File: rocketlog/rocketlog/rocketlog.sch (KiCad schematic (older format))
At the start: 14 parts, among them J1 Conn_01x05_Female, U1 DSPIC33EP512GP502, U2 MCP2562, Y1 Crystal

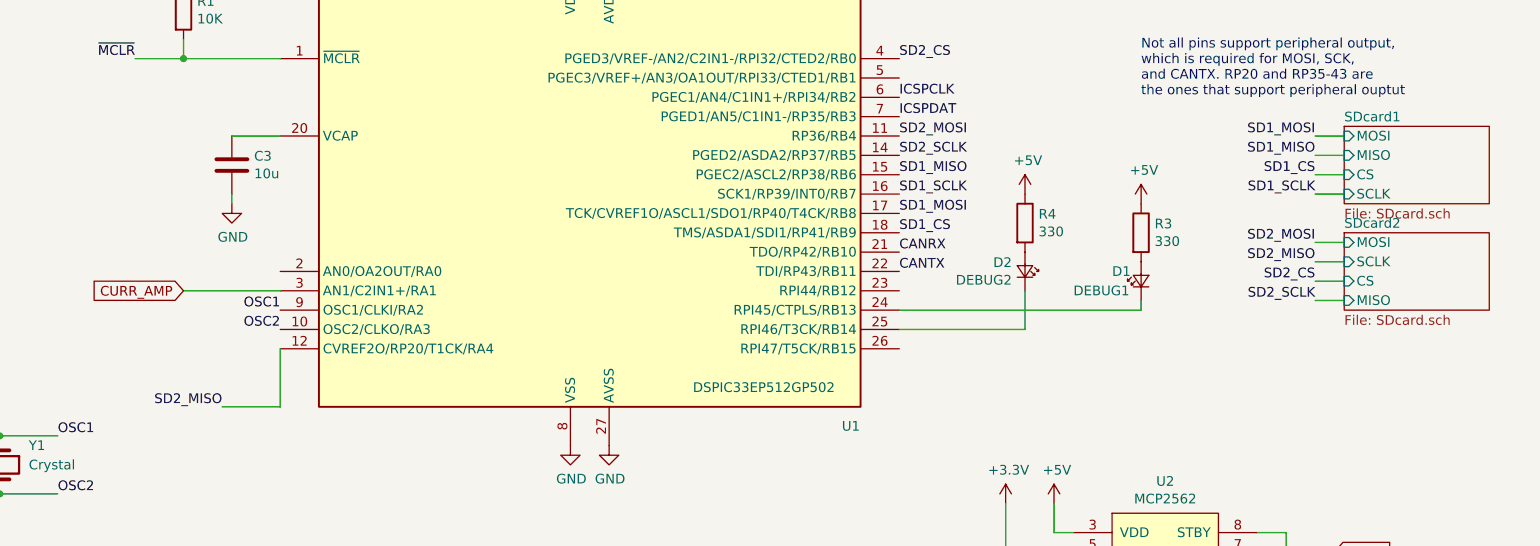
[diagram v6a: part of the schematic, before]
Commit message: Logger Board: Add pullup resistors on SD card MISO lines
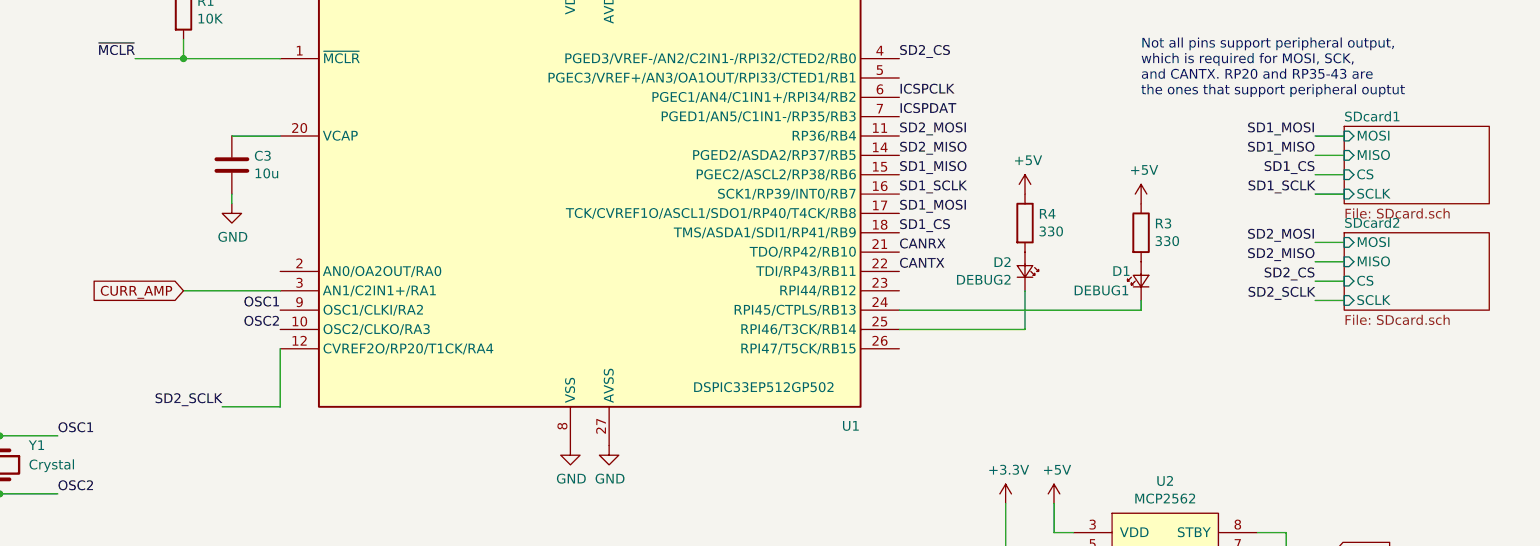
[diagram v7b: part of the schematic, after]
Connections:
- net SD2_MISO: now also U1.14 (PGED2/ASDA2/RP37/RB5); no longer U1.12 (CVREF2O/RP20/T1CK/RA4)
- net SD2_SCLK: now also U1.12 (CVREF2O/RP20/T1CK/RA4); no longer U1.14 (PGED2/ASDA2/RP37/RB5)
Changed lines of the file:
@@
 F0 "SDcard2" 50
 F1 "SDcard.sch" 50
-F2 "MISO" I L 9700 4500 50
+F2 "MISO" I L 9700 4300 50
 F3 "MOSI" I L 9700 4200 50
-F4 "SCLK" I L 9700 4300 50
+F4 "SCLK" I L 9700 4500 50
 F5 "CS" I L 9700 4400 50
 $EndSheet
@@
 Text Label 7400 3650 0    50   ~ 0
 SD2_MOSI
-Text Label 3900 5050 2    50   ~ 0
+Text Label 7400 3750 0    50   ~ 0
 SD2_MISO
 Text Label 7400 3250 0    50   ~ 0
 SD2_CS
-Text Label 7400 3750 0    50   ~ 0
+Text Label 3900 5050 2    50   ~ 0
 SD2_SCLK
 Text Label 7400 4350 0    50   ~ 0

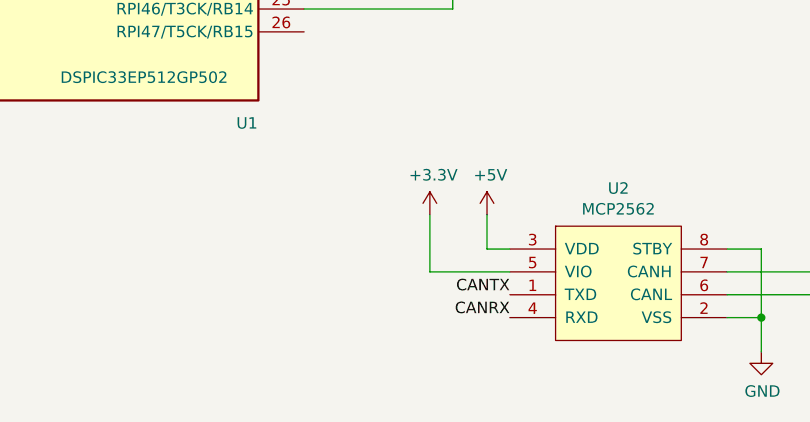
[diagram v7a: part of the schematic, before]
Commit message: Logger Board: Fab review 1 fixes
Changes fixed in this commit:
  - Make mounting holes 1.5in square because I ain't no metric apologist
  - Make programming header not overhang bottom right mounting hole
  - Change MCLR to ~MCLR on silkscreen
  - Move C1 closer to MCU
  - Move C3 further from MCU
  - Add 10uF capacitor on CAN transceiver (C11)

Generate gerbers to reflect these changes
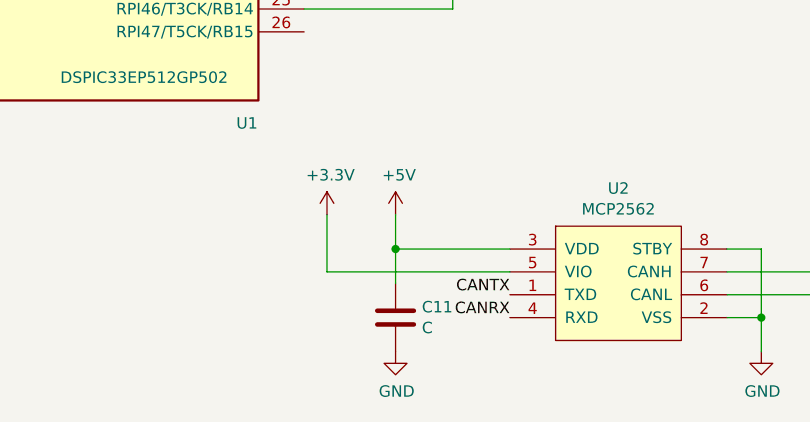
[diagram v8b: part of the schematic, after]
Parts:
- added C11: C, Capacitor_SMD:C_0805_2012Metric_Pad1.15x1.40mm_HandSolder, symbol Device:C
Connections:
- net +5V: now also C11.1
- net GND: now also C11.2
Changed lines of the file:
@@
 L power:+5V #PWR015
 U 1 1 5B9EA857
-P 8200 5550
-F 0 "#PWR015" H 8200 5400 50  0001 C CNN
-F 1 "+5V" H 8215 5723 50  0000 C CNN
-F 2 "" H 8200 5550 50  0001 C CNN
-F 3 "" H 8200 5550 50  0001 C CNN
-	1    8200 5550
+P 7800 5550
+F 0 "#PWR015" H 7800 5400 50  0001 C CNN
+F 1 "+5V" H 7815 5723 50  0000 C CNN
+F 2 "" H 7800 5550 50  0001 C CNN
+F 3 "" H 7800 5550 50  0001 C CNN
+	1    7800 5550
 	1    0    0    -1
 $EndComp
@@
 L power:+3.3V #PWR014
 U 1 1 5B9EA85D
-P 7950 5550
-F 0 "#PWR014" H 7950 5400 50  0001 C CNN
-F 1 "+3.3V" H 7965 5723 50  0000 C CNN
-F 2 "" H 7950 5550 50  0001 C CNN
-F 3 "" H 7950 5550 50  0001 C CNN
-	1    7950 5550
-	1    0    0    -1
-$EndComp
-Wire Wire Line
-	7950 5550 7950 5800
-Wire Wire Line
-	7950 5800 8300 5800
-Wire Wire Line
-	8200 5550 8200 5700
-Wire Wire Line
-	8200 5700 8300 5700
+P 7500 5550
+F 0 "#PWR014" H 7500 5400 50  0001 C CNN
+F 1 "+3.3V" H 7515 5723 50  0000 C CNN
+F 2 "" H 7500 5550 50  0001 C CNN
+F 3 "" H 7500 5550 50  0001 C CNN
+	1    7500 5550
+	1    0    0    -1
+$EndComp
+Wire Wire Line
+	7500 5550 7500 5800
+Wire Wire Line
+	7500 5800 8300 5800
+Wire Wire Line
+	7800 5550 7800 5700
+Wire Wire Line
+	7800 5700 8300 5700
 $Comp
 L power:GND #PWR016
@@
 Wire Wire Line
 	8050 4650 7400 4650
+$Comp
+L Device:C C11
+U 1 1 5BDE69DD
+P 7800 6000
+F 0 "C11" H 7915 6046 50  0000 L CNN
+F 1 "C" H 7915 5955 50  0000 L CNN
+F 2 "Capacitor_SMD:C_0805_2012Metric_Pad1.15x1.40mm_HandSolder" H 7838 5850 50  0001 C CNN
+F 3 "~" H 7800 6000 50  0001 C CNN
+	1    7800 6000
+	1    0    0    -1
+$EndComp
+Wire Wire Line
+	7800 5850 7800 5700
+Connection ~ 7800 5700
+$Comp
+L power:GND #PWR035
+U 1 1 5BDE912B
+P 7800 6150
+F 0 "#PWR035" H 7800 5900 50  0001 C CNN
+F 1 "GND" H 7805 5977 50  0000 C CNN
+F 2 "" H 7800 6150 50  0001 C CNN
+F 3 "" H 7800 6150 50  0001 C CNN
+	1    7800 6150
+	1    0    0    -1
+$EndComp
 $EndSCHEMATC
